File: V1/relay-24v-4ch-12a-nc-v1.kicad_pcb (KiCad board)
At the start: 2 copper layers, 68 x 67.8 mm, 24 parts, among them J1 DB141V-2.54-2P, J2 DB141V-2.54-4P, J3 DB142V-5.08-4P, J4 DB142V-5.08-4P, K1 Songle_SRD_1B, K2 Songle_SRD_1B, K3 Songle_SRD_1B, K4 Songle_SRD_1B

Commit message: Review before fabrication
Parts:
- R1, R2, R3, R4: value 6k8/100mW -> 10k/100mW
- moved R1 26.1 mm to (159.2, 65.2), turned to -90 degrees
- moved R2 23.3 mm to (161.0, 65.2), turned to -90 degrees
- moved R3 20.1 mm to (162.8, 65.2), turned to -90 degrees
- moved R4 16.9 mm to (164.5, 65.2), turned to -90 degrees
- moved J3 8.39 mm to (145.5, 118.8)
- moved J4 8.39 mm to (177.5, 118.8)
- moved K1 7.25 mm to (135.0, 89.8)
- moved K2 7.25 mm to (151.0, 89.8)
- moved K3 7.25 mm to (167.0, 89.8)
- moved K4 7.25 mm to (183.0, 89.8)
- moved J2 4.65 mm to (174.2, 70.5)
- moved D2 3.29 mm to (128.2, 79.8)
- moved D4 3.29 mm to (144.2, 79.8)
- moved D6 3.29 mm to (160.2, 79.8)
- moved D8 3.29 mm to (176.2, 79.8)
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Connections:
- net Net-(D1-A) renamed /LED1
- net Net-(D1-K) renamed /IN1
- net Net-(D3-A) renamed /LED2
- net Net-(D3-K) renamed /IN2
- net Net-(D5-A) renamed /LED3
- net Net-(D5-K) renamed /IN3
- net Net-(D7-A) renamed /LED4
- net Net-(D7-K) renamed /IN4
- net Net-(J3-Pin_1) renamed /OUT1PW
- net Net-(J3-Pin_2) renamed /OUT1LD
- net Net-(J3-Pin_3) renamed /OUT2PW
- net Net-(J3-Pin_4) renamed /OUT2LD
- net Net-(J4-Pin_1) renamed /OUT3PW
- net Net-(J4-Pin_2) renamed /OUT3LD
- net Net-(J4-Pin_3) renamed /OUT4PW
- net Net-(J4-Pin_4) renamed /OUT4LD
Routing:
- net +24V: track 197.3 -> 138.1 mm
- net /LED1: track 2.03 -> 26.8 mm
- net /IN2: track 58.9 -> 82.3 mm
- net /LED2: track 2.03 -> 24.1 mm
- net /LED3: track 2.03 -> 20.9 mm
- net /LED4: track 2.03 -> 17.6 mm
- net /IN4: track 75.3 -> 62.5 mm
- net /IN3: track 58.5 -> 66.3 mm
- net /IN1: track 65.6 -> 63.9 mm
- added copper zone on F.Cu, net +24V
- removed copper zone on B.Cu, net +24V
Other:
- rule pad_to_mask_clearance: 0 -> 0.1

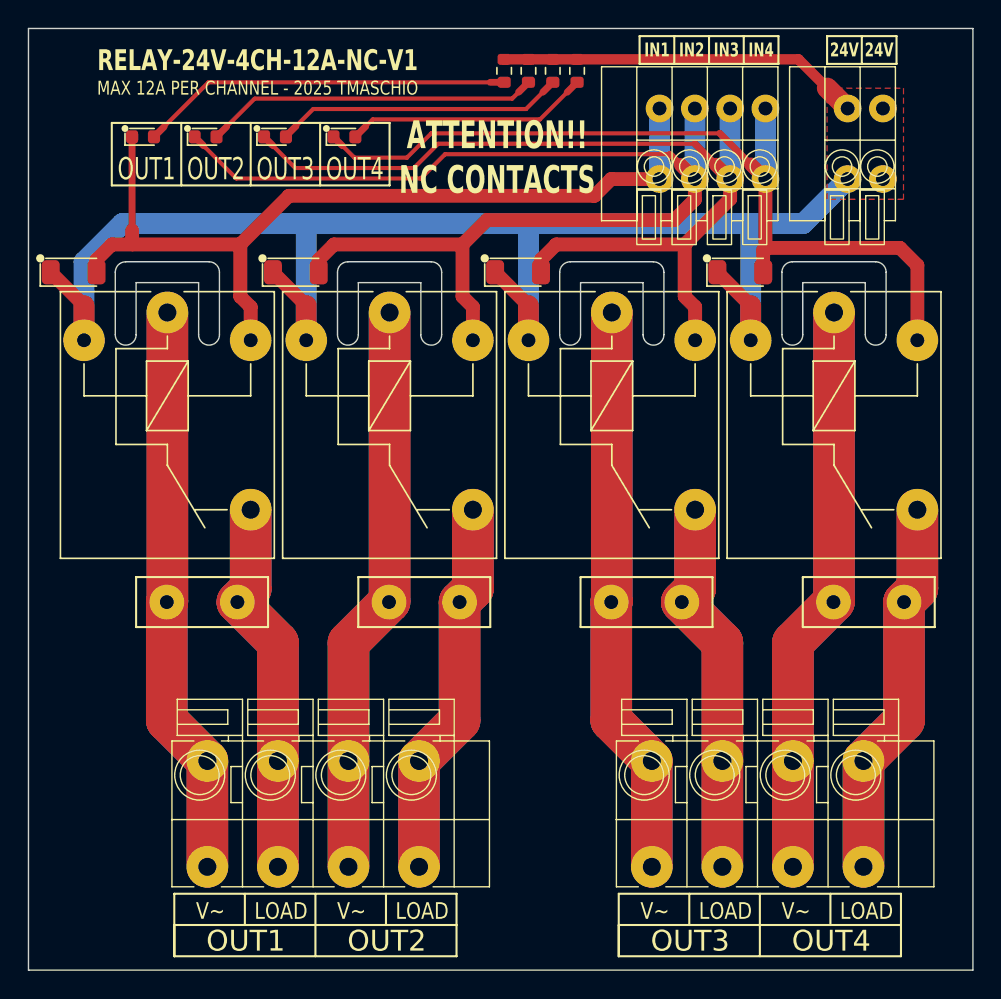
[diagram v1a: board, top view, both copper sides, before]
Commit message: Replaced input terminal blocks for 3.5mm pitch.
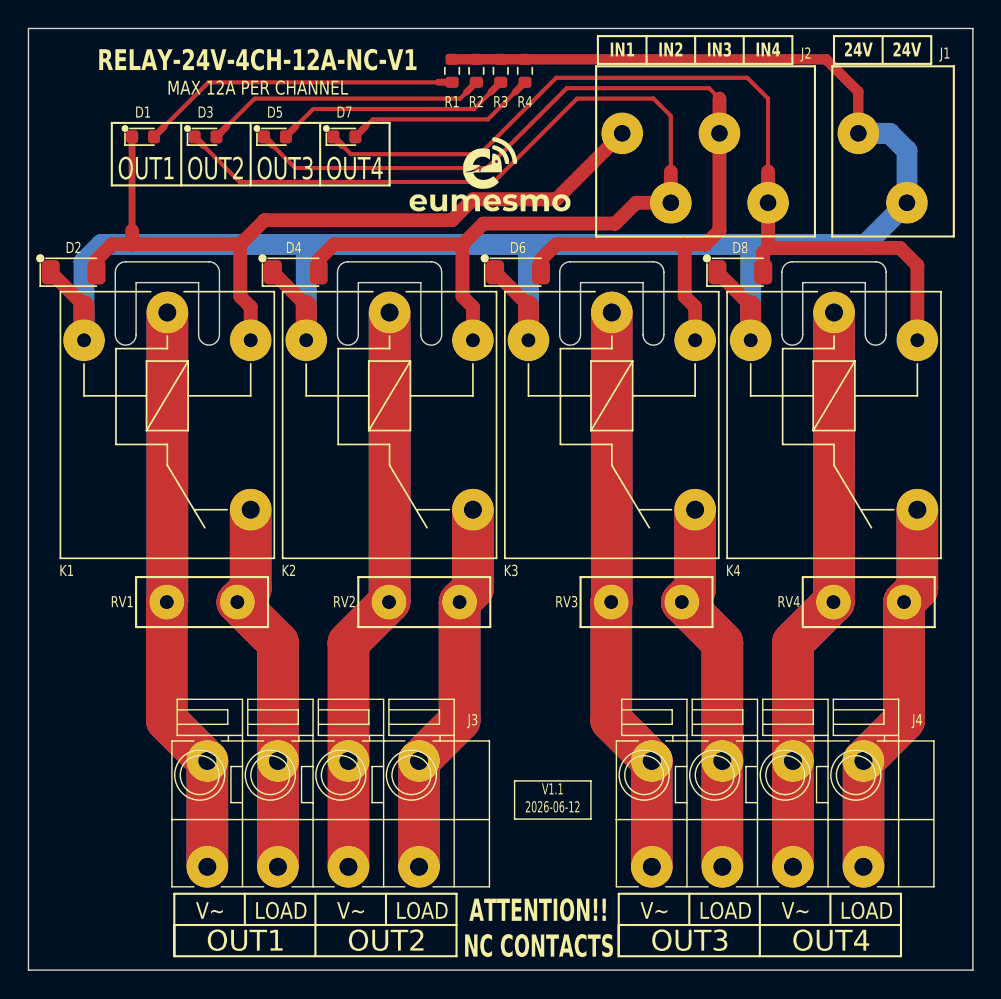
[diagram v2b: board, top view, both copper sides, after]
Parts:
- added G***: LOGO, Tales:Eumesmo_small_silk, F.Cu at (158.2, 72.8)
- J1: value DB141V-2.54-2P -> 250-202; footprint Tales:TerminalBlock_Dibo_DB141V-2.54-2P_1x02_P2.54mm_Vertical -> Tales:TerminalBlock_Wago_250-202_1x02_P3.5mm_45Degree
- J2: value DB141V-2.54-4P -> 250-204; footprint Tales:TerminalBlock_Dibo_DB141V-2.54-4P_1x04_P2.54mm_Vertical -> Tales:TerminalBlock_Wago_250-204_1x04_P3.5mm_45Degree
- moved R1 3.75 mm to (155.5, 65.2)
- moved R2 3.75 mm to (157.2, 65.2)
- moved R3 3.75 mm to (159.0, 65.2)
- moved R4 3.75 mm to (160.8, 65.2)
- moved J1 2.15 mm to (186.5, 72.2)
- moved J2 2.15 mm to (173.0, 72.2)
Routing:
- net +24V: track 138.1 -> 151.9 mm
- net /IN1: track 63.9 -> 57.5 mm
- net /LED4: track 17.6 -> 13.8 mm
- net /LED3: track 20.9 -> 17.1 mm
- net /LED2: track 24.1 -> 20.3 mm
- net /LED1: track 26.8 -> 23.1 mm
- net /IN2: track 82.3 -> 80.0 mm
- net /IN4: track 62.5 -> 64.0 mm
- net /IN3: track 66.3 -> 67.7 mm
- removed copper zone on F.Cu, net +24V
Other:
- board text added: "MAX 12A PER CHANNEL"
- board text added: "V1.1 2026-06-12"
- board text removed: "MAX 12A PER CHANNEL - 2025 TMASCHIO"

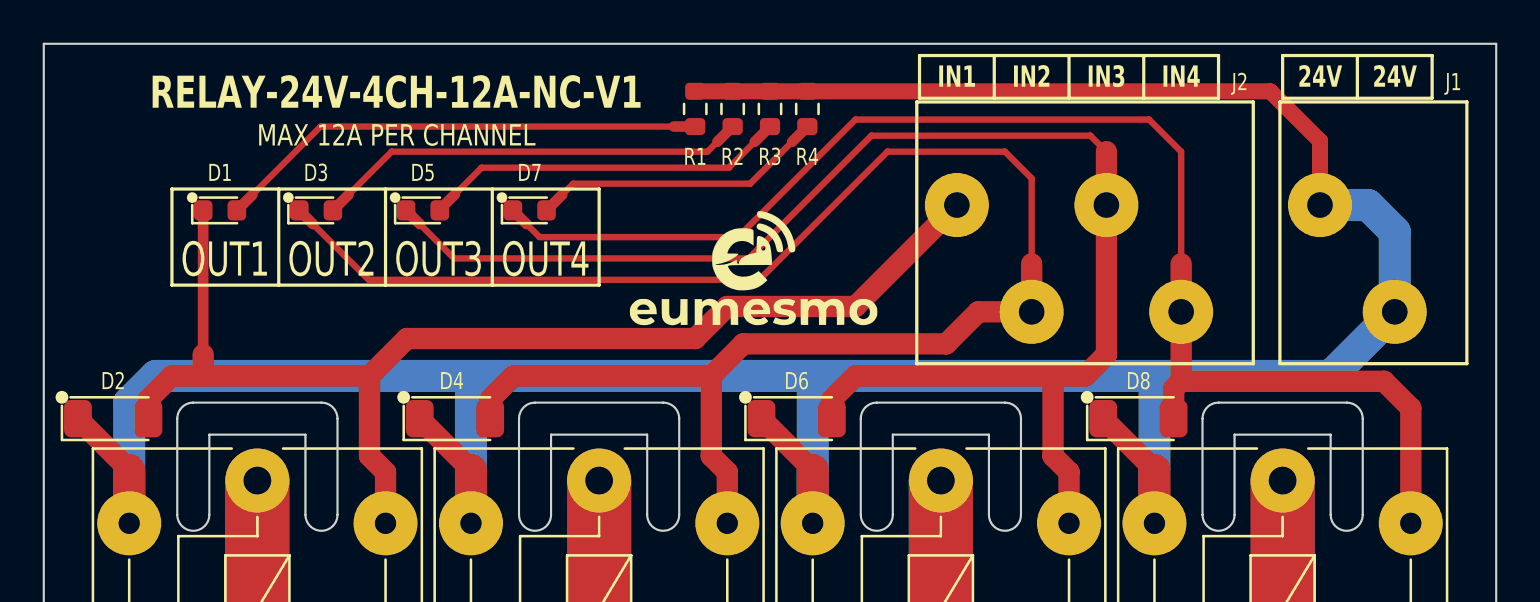
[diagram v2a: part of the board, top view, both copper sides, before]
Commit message: Small adjustments to silkscreen
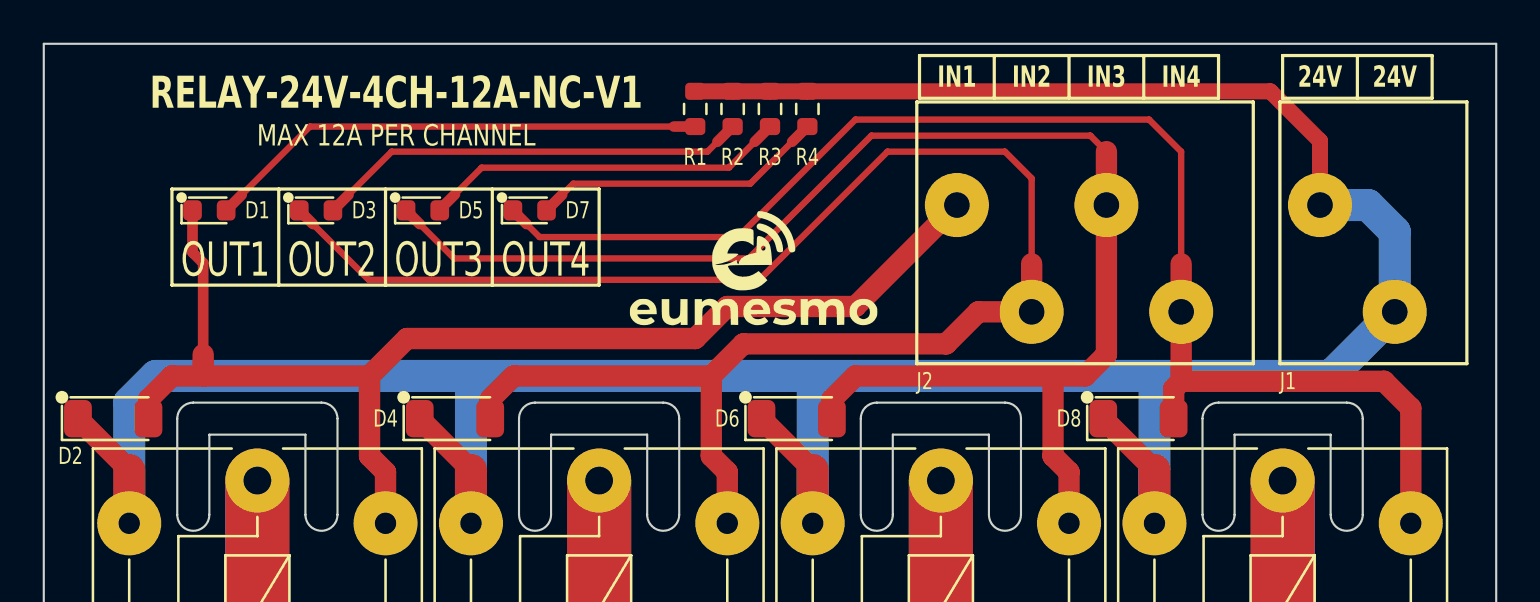
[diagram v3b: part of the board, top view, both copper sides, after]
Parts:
- moved D1 0.50 mm to (132.8, 70.0)
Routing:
- net /LED1: track 23.1 -> 23.6 mm
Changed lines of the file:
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@@
 		(tags "SOD-123")
 		(property "Reference" "D4"
-			(at -0.15 -1.75 0)
+			(at -3.25 0 0)
 			(layer "F.SilkS")
 			(effects
@@
 		(tags "LED")
 		(property "Reference" "D7"
-			(at 0 -1.75 0)
+			(at 2.25 0 0)
 			(layer "F.SilkS")
 			(effects
@@
 		(tags "250-204 ")
 		(property "Reference" "J2"
-			(at -8 8.25 0)
+			(at 6.75 -5.75 0)
 			(unlocked yes)
 			(layer "F.SilkS")
@@
 	(footprint "Tales:LED_0603_1608Metric"
 		(layer "F.Cu")
-		(at 133.25 70)
+		(at 132.75 70)
 		(descr "LED SMD 0603 (1608 Metric), square (rectangular) end terminal, IPC_7351 nominal, (Body size source: http://www.tortai-tech.com/upload/download/2011102023233369053.pdf), generated with kicad-footprint-generator")
 		(tags "LED")
 		(property "Reference" "D1"
-			(at 0 -1.75 0)
+			(at 2.25 0 0)
 			(layer "F.SilkS")
 			(effects
@@
 		(tags "SOD-123")
 		(property "Reference" "D2"
-			(at 0 -1.75 0)
+			(at -2 1.75 0)
 			(layer "F.SilkS")
 			(effects
@@
 		(tags "SOD-123")
 		(property "Reference" "D6"
-			(at 0 -1.75 0)
+			(at -3.25 0 0)
 			(layer "F.SilkS")
 			(effects
@@
 		(tags "LED")
 		(property "Reference" "D3"
-			(at 0 -1.75 0)
+			(at 2.25 0 0)
 			(layer "F.SilkS")
 			(effects
@@
 		(tags "250-202 ")
 		(property "Reference" "J1"
-			(at -4.5 8.25 0)
+			(at 3.25 -5.75 0)
 			(unlocked yes)
 			(layer "F.SilkS")
@@
 		(tags "SOD-123")
 		(property "Reference" "D8"
-			(at 0 -1.75 0)
+			(at -3.25 0 0)
 			(layer "F.SilkS")
 			(effects
@@
 		(tags "LED")
 		(property "Reference" "D5"
-			(at 0 -1.75 0)
+			(at 2.25 0 0)
 			(layer "F.SilkS")
 			(effects
@@
 	)
 	(segment
+		(start 131.9625 71.9625)
+		(end 131.9625 70)
+		(width 0.5)
+		(layer "F.Cu")
+		(net "/IN1")
+	)
+	(segment
 		(start 141 84.65)
 		(end 141 82.25)
@@
 	)
 	(segment
+		(start 132.4625 72.4625)
+		(end 131.9625 71.9625)
+		(width 0.5)
+		(layer "F.Cu")
+		(net "/IN1")
+	)
+	(segment
 		(start 155.5 76)
 		(end 157 74.5)
@@
 	)
 	(segment
+		(start 132.4625 76.75)
+		(end 132.4625 72.4625)
+		(width 0.5)
+		(layer "F.Cu")
+		(net "/IN1")
+	)
+	(segment
 		(start 163 74.5)
 		(end 167.75 69.75)
@@
 	)
 	(segment
-		(start 132.4625 70)
-		(end 132.4625 76.75)
+		(start 154.5 66.075)
+		(end 155.5 66.075)
 		(width 0.5)
 		(layer "F.Cu")
-		(net "/IN1")
+		(net "/LED1")
 	)
 	(segment
-		(start 134.76875 69.26875)
-		(end 137.9625 66.075)
+		(start 134.26875 69.26875)
+		(end 137.4625 66.075)
 		(width 0.3)
 		(layer "F.Cu")
@@
 	)
 	(segment
-		(start 154.5 66.075)
-		(end 155.5 66.075)
+		(start 133.5375 70)
+		(end 134.26875 69.26875)
 		(width 0.5)
 		(layer "F.Cu")
@@
 	)
 	(segment
-		(start 137.9625 66.075)
+		(start 137.4625 66.075)
 		(end 154.5 66.075)
 		(width 0.3)
 		(layer "F.Cu")
 		(net "/LED1")
-	)
-	(segment
-		(start 134.0375 70)
-		(end 134.76875 69.26875)
-		(width 0.5)
-		(layer "F.Cu")
-		(net "/LED1")
